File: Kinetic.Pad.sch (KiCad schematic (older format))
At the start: 18 parts, among them SW1 Rotary_Encoder_Switch, U1 ProMicro

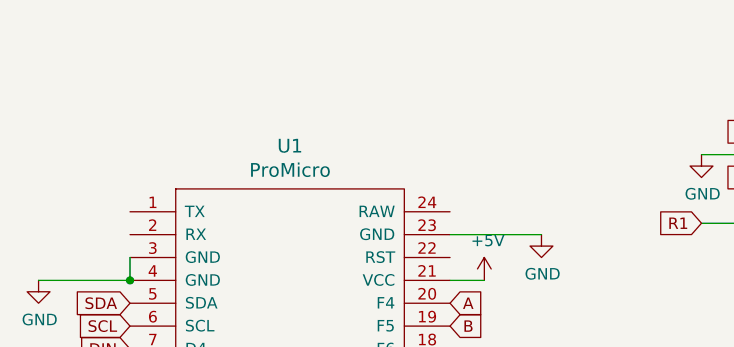
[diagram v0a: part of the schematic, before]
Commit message: Updated MX Libraries
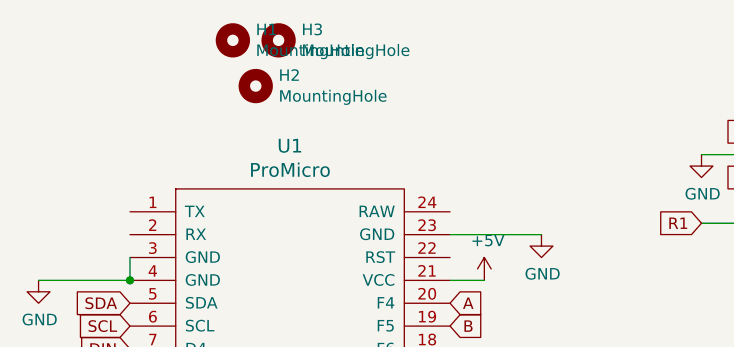
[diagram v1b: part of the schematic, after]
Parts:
- added H1, H2, H3: MountingHole, MountingHole:MountingHole_2mm, symbol Mechanical:MountingHole
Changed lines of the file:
@@
 Wire Wire Line
 	5150 3900 5700 3900
+$Comp
+L Mechanical:MountingHole H1
+U 1 1 61AF6BAE
+P 2350 950
+F 0 "H1" H 2450 996 50  0000 L CNN
+F 1 "MountingHole" H 2450 905 50  0000 L CNN
+F 2 "MountingHole:MountingHole_2mm" H 2350 950 50  0001 C CNN
+F 3 "~" H 2350 950 50  0001 C CNN
+	1    2350 950
+	1    0    0    -1
+$EndComp
+$Comp
+L Mechanical:MountingHole H3
+U 1 1 61AF77EB
+P 2550 950
+F 0 "H3" H 2650 996 50  0000 L CNN
+F 1 "MountingHole" H 2650 905 50  0000 L CNN
+F 2 "MountingHole:MountingHole_2mm" H 2550 950 50  0001 C CNN
+F 3 "~" H 2550 950 50  0001 C CNN
+	1    2550 950
+	1    0    0    -1
+$EndComp
+$Comp
+L Mechanical:MountingHole H2
+U 1 1 61AF7FA8
+P 2450 1150
+F 0 "H2" H 2550 1196 50  0000 L CNN
+F 1 "MountingHole" H 2550 1105 50  0000 L CNN
+F 2 "MountingHole:MountingHole_2mm" H 2450 1150 50  0001 C CNN
+F 3 "~" H 2450 1150 50  0001 C CNN
+	1    2450 1150
+	1    0    0    -1
+$EndComp
 $EndSCHEMATC

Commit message: Switched Libraries, Deleted Old Gerbers, Deleted Old Step FIle
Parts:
- MX1, MX2, MX3, MX4, MX5: footprint MX_Alps_Hybrid:MX-1U-NoLED -> MX_Only:MXOnly-1U-NoLED
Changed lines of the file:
@@
 F 0 "MX1" H 4583 2973 60  0000 C CNN
 F 1 "MX-NoLED" H 4583 2899 20  0000 C CNN
-F 2 "MX_Alps_Hybrid:MX-1U-NoLED" H 3925 2725 60  0001 C CNN
+F 2 "MX_Only:MXOnly-1U-NoLED" H 3925 2725 60  0001 C CNN
 F 3 "" H 3925 2725 60  0001 C CNN
 	1    4550 2750
@@
 F 0 "MX3" H 5033 2973 60  0000 C CNN
 F 1 "MX-NoLED" H 5033 2899 20  0000 C CNN
-F 2 "MX_Alps_Hybrid:MX-1U-NoLED" H 4375 2725 60  0001 C CNN
+F 2 "MX_Only:MXOnly-1U-NoLED" H 4375 2725 60  0001 C CNN
 F 3 "" H 4375 2725 60  0001 C CNN
 	1    5000 2750
@@
 F 0 "MX5" H 5483 2973 60  0000 C CNN
 F 1 "MX-NoLED" H 5483 2899 20  0000 C CNN
-F 2 "MX_Alps_Hybrid:MX-1U-NoLED" H 4825 2725 60  0001 C CNN
+F 2 "MX_Only:MXOnly-1U-NoLED" H 4825 2725 60  0001 C CNN
 F 3 "" H 4825 2725 60  0001 C CNN
 	1    5450 2750
@@
 F 0 "MX4" H 5483 2323 60  0000 C CNN
 F 1 "MX-NoLED" H 5483 2249 20  0000 C CNN
-F 2 "MX_Alps_Hybrid:MX-1U-NoLED" H 4825 2075 60  0001 C CNN
+F 2 "MX_Only:MXOnly-1U-NoLED" H 4825 2075 60  0001 C CNN
 F 3 "" H 4825 2075 60  0001 C CNN
 	1    5450 2100
@@
 F 0 "MX2" H 5033 2323 60  0000 C CNN
 F 1 "MX-NoLED" H 5033 2249 20  0000 C CNN
-F 2 "MX_Alps_Hybrid:MX-1U-NoLED" H 4375 2075 60  0001 C CNN
+F 2 "MX_Only:MXOnly-1U-NoLED" H 4375 2075 60  0001 C CNN
 F 3 "" H 4375 2075 60  0001 C CNN
 	1    5000 2100

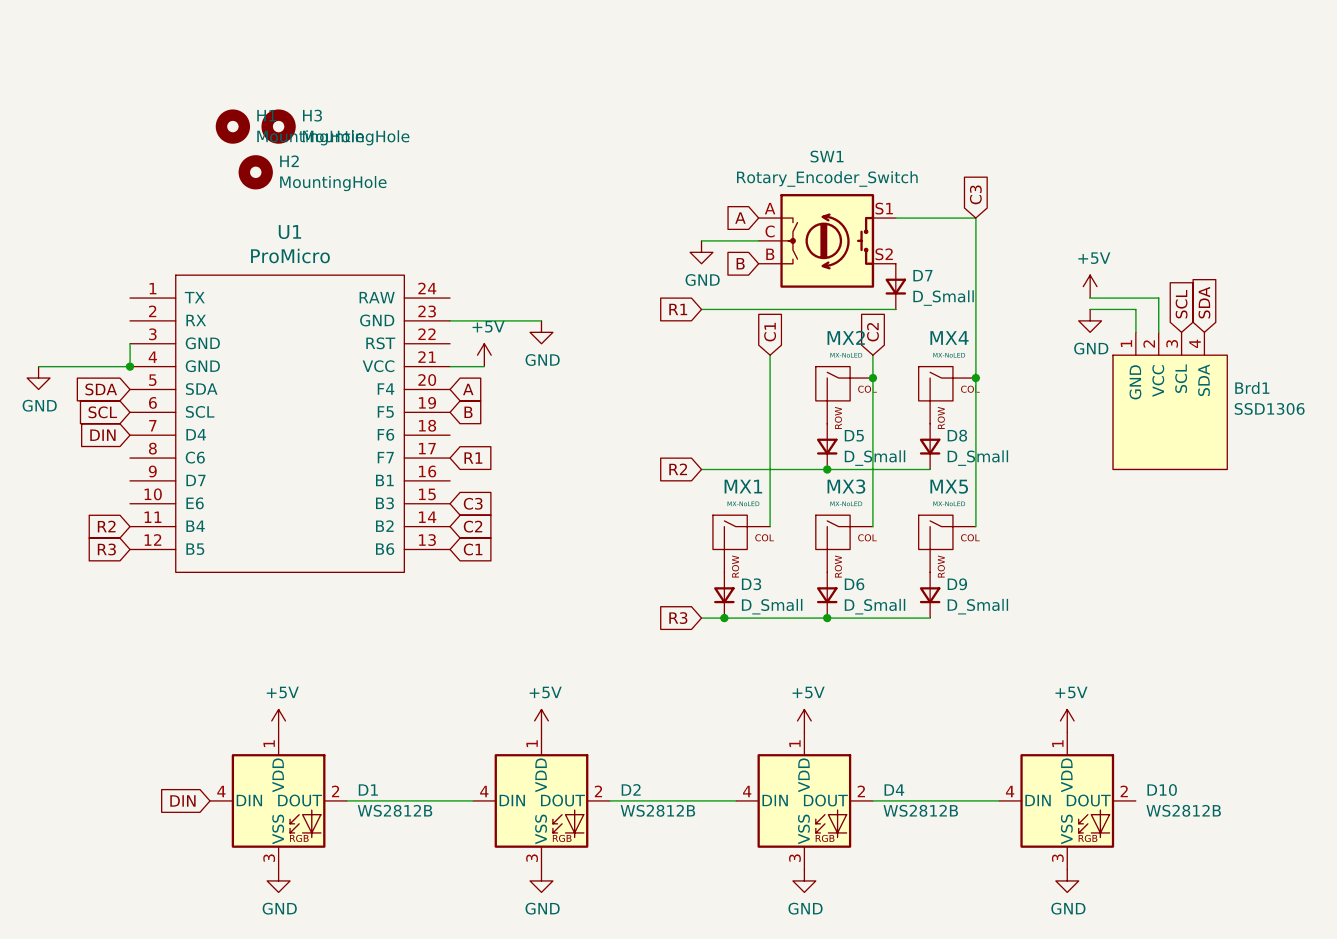
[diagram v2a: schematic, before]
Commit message: Removed Old Gerbers
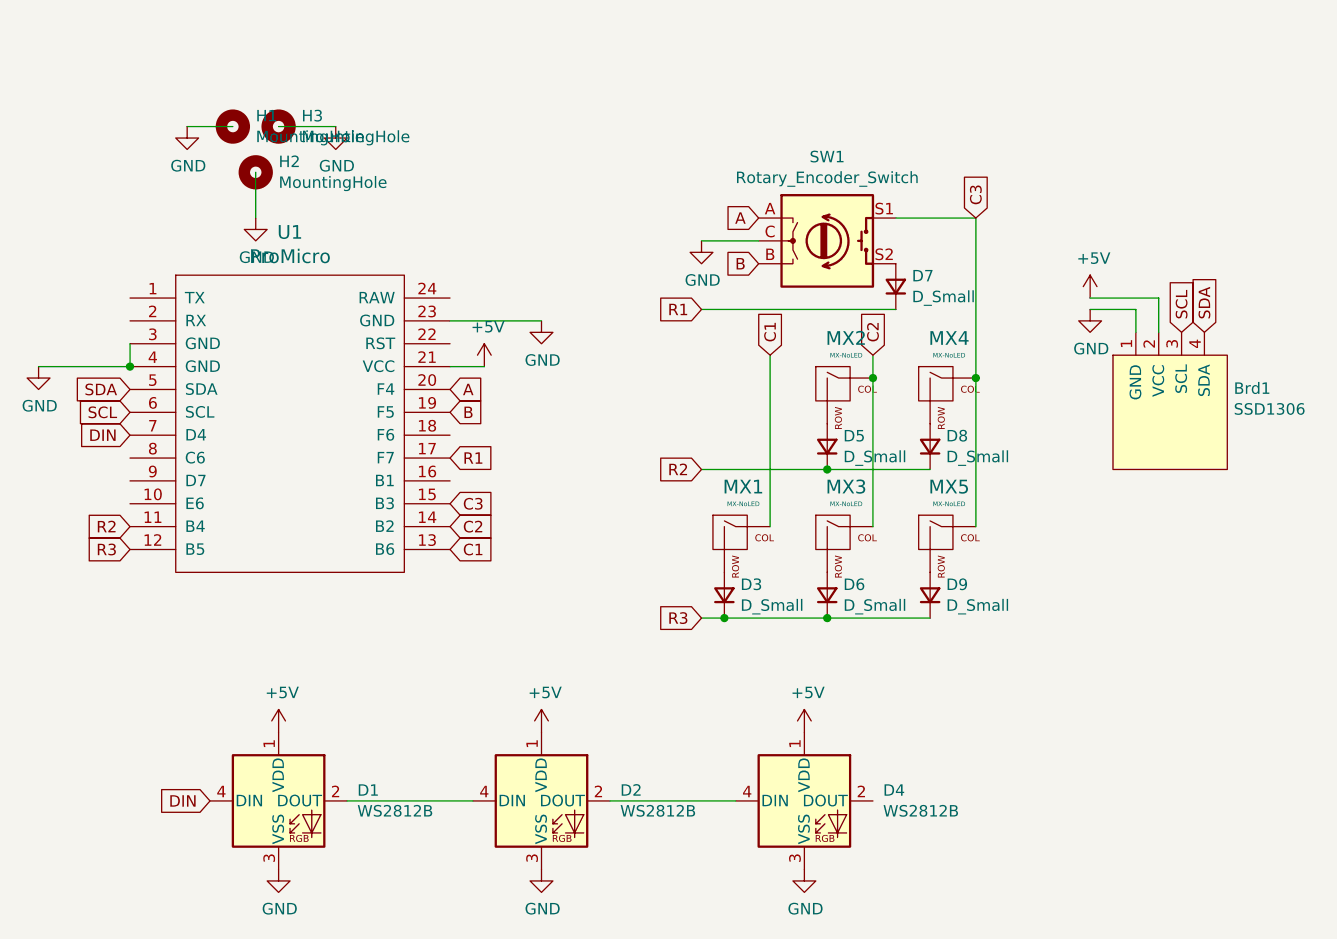
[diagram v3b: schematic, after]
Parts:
- removed D10: WS2812B, LED_SMD:LED_WS2812B_PLCC4_5.0x5.0mm_P3.2mm, symbol LED:WS2812B
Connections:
- wire segments 24 -> 26
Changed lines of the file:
@@
-$EndComp
-$Comp
-L LED:WS2812B D10
-U 1 1 61A89769
-P 6000 3900
-F 0 "D10" H 6344 3946 50  0000 L CNN
-F 1 "WS2812B" H 6344 3855 50  0000 L CNN
-F 2 "LED_SMD:LED_WS2812B_PLCC4_5.0x5.0mm_P3.2mm" H 6050 3600 50  0001 L TNN
-F 3 "https://cdn-shop.adafruit.com/datasheets/WS2812B.pdf" H 6100 3525 50  0001 L TNN
-	1    6000 3900
-	1    0    0    -1
 $EndComp
 $Comp
@@
 F 3 "" H 4850 4200 50  0001 C CNN
 	1    4850 4200
-	1    0    0    -1
-$EndComp
-$Comp
-L power:GND #PWR0110
-U 1 1 61A8B838
-P 6000 4200
-F 0 "#PWR0110" H 6000 3950 50  0001 C CNN
-F 1 "GND" H 6005 4027 50  0000 C CNN
-F 2 "" H 6000 4200 50  0001 C CNN
-F 3 "" H 6000 4200 50  0001 C CNN
-	1    6000 4200
-	1    0    0    -1
-$EndComp
-$Comp
-L power:+5V #PWR0111
-U 1 1 61A8BD21
-P 6000 3600
-F 0 "#PWR0111" H 6000 3450 50  0001 C CNN
-F 1 "+5V" H 6015 3773 50  0000 C CNN
-F 2 "" H 6000 3600 50  0001 C CNN
-F 3 "" H 6000 3600 50  0001 C CNN
-	1    6000 3600
 	1    0    0    -1
 $EndComp
@@
 Wire Wire Line
 	4000 3900 4550 3900
-Wire Wire Line
-	5150 3900 5700 3900
 $Comp
 L Mechanical:MountingHole H1
@@
 	1    0    0    -1
 $EndComp
+Wire Wire Line
+	2550 950  2800 950
+Wire Wire Line
+	2450 1150 2450 1350
+Wire Wire Line
+	2350 950  2150 950
+$Comp
+L power:GND #PWR0110
+U 1 1 61A99687
+P 2800 950
+F 0 "#PWR0110" H 2800 700 50  0001 C CNN
+F 1 "GND" H 2805 777 50  0000 C CNN
+F 2 "" H 2800 950 50  0001 C CNN
+F 3 "" H 2800 950 50  0001 C CNN
+	1    2800 950
+	1    0    0    -1
+$EndComp
+$Comp
+L power:GND #PWR0111
+U 1 1 61A99FC8
+P 2450 1350
+F 0 "#PWR0111" H 2450 1100 50  0001 C CNN
+F 1 "GND" H 2455 1177 50  0000 C CNN
+F 2 "" H 2450 1350 50  0001 C CNN
+F 3 "" H 2450 1350 50  0001 C CNN
+	1    2450 1350
+	1    0    0    -1
+$EndComp
+$Comp
+L power:GND #PWR0115
+U 1 1 61A9A984
+P 2150 950
+F 0 "#PWR0115" H 2150 700 50  0001 C CNN
+F 1 "GND" H 2155 777 50  0000 C CNN
+F 2 "" H 2150 950 50  0001 C CNN
+F 3 "" H 2150 950 50  0001 C CNN
+	1    2150 950
+	1    0    0    -1
+$EndComp

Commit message: Nothing Important
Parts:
- removed H1, H2, H3: MountingHole, MountingHole:MountingHole_2mm, symbol Mechanical:MountingHole
- added H1, H2, H3: MountingHole_Pad, MountingHole:MountingHole_2.5mm_Pad, symbol Mechanical:MountingHole_Pad
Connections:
- wire segments 26 -> 23
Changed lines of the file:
@@
 	4000 3900 4550 3900
 $Comp
-L Mechanical:MountingHole H1
-U 1 1 61AF6BAE
-P 2350 950
-F 0 "H1" H 2450 996 50  0000 L CNN
-F 1 "MountingHole" H 2450 905 50  0000 L CNN
-F 2 "MountingHole:MountingHole_2mm" H 2350 950 50  0001 C CNN
-F 3 "~" H 2350 950 50  0001 C CNN
-	1    2350 950
+L Mechanical:MountingHole_Pad H1
+U 1 1 61A9C773
+P 1700 1050
+F 0 "H1" H 1800 1099 50  0000 L CNN
+F 1 "MountingHole_Pad" H 1800 1008 50  0000 L CNN
+F 2 "MountingHole:MountingHole_2.5mm_Pad" H 1700 1050 50  0001 C CNN
+F 3 "~" H 1700 1050 50  0001 C CNN
+	1    1700 1050
 	1    0    0    -1
 $EndComp
 $Comp
-L Mechanical:MountingHole H3
-U 1 1 61AF77EB
-P 2550 950
-F 0 "H3" H 2650 996 50  0000 L CNN
-F 1 "MountingHole" H 2650 905 50  0000 L CNN
-F 2 "MountingHole:MountingHole_2mm" H 2550 950 50  0001 C CNN
-F 3 "~" H 2550 950 50  0001 C CNN
-	1    2550 950
+L Mechanical:MountingHole_Pad H3
+U 1 1 61A9D1A0
+P 1900 1050
+F 0 "H3" H 2000 1099 50  0000 L CNN
+F 1 "MountingHole_Pad" H 2000 1008 50  0000 L CNN
+F 2 "MountingHole:MountingHole_2.5mm_Pad" H 1900 1050 50  0001 C CNN
+F 3 "~" H 1900 1050 50  0001 C CNN
+	1    1900 1050
 	1    0    0    -1
 $EndComp
 $Comp
-L Mechanical:MountingHole H2
-U 1 1 61AF7FA8
-P 2450 1150
-F 0 "H2" H 2550 1196 50  0000 L CNN
-F 1 "MountingHole" H 2550 1105 50  0000 L CNN
-F 2 "MountingHole:MountingHole_2mm" H 2450 1150 50  0001 C CNN
-F 3 "~" H 2450 1150 50  0001 C CNN
-	1    2450 1150
+L Mechanical:MountingHole_Pad H2
+U 1 1 61A9D90B
+P 1800 600
+F 0 "H2" H 1900 649 50  0000 L CNN
+F 1 "MountingHole_Pad" H 1900 558 50  0000 L CNN
+F 2 "MountingHole:MountingHole_2.5mm_Pad" H 1800 600 50  0001 C CNN
+F 3 "~" H 1800 600 50  0001 C CNN
+	1    1800 600
 	1    0    0    -1
 $EndComp
-Wire Wire Line
-	2550 950  2800 950
-Wire Wire Line
-	2450 1150 2450 1350
-Wire Wire Line
-	2350 950  2150 950
 $Comp
 L power:GND #PWR0110
-U 1 1 61A99687
-P 2800 950
-F 0 "#PWR0110" H 2800 700 50  0001 C CNN
-F 1 "GND" H 2805 777 50  0000 C CNN
-F 2 "" H 2800 950 50  0001 C CNN
-F 3 "" H 2800 950 50  0001 C CNN
-	1    2800 950
+U 1 1 61AA5B29
+P 1700 1150
+F 0 "#PWR0110" H 1700 900 50  0001 C CNN
+F 1 "GND" H 1705 977 50  0000 C CNN
+F 2 "" H 1700 1150 50  0001 C CNN
+F 3 "" H 1700 1150 50  0001 C CNN
+	1    1700 1150
 	1    0    0    -1
 $EndComp
 $Comp
 L power:GND #PWR0111
-U 1 1 61A99FC8
-P 2450 1350
-F 0 "#PWR0111" H 2450 1100 50  0001 C CNN
-F 1 "GND" H 2455 1177 50  0000 C CNN
-F 2 "" H 2450 1350 50  0001 C CNN
-F 3 "" H 2450 1350 50  0001 C CNN
-	1    2450 1350
+U 1 1 61AA6232
+P 1900 1150
+F 0 "#PWR0111" H 1900 900 50  0001 C CNN
+F 1 "GND" H 1905 977 50  0000 C CNN
+F 2 "" H 1900 1150 50  0001 C CNN
+F 3 "" H 1900 1150 50  0001 C CNN
+	1    1900 1150
 	1    0    0    -1
 $EndComp
 $Comp
 L power:GND #PWR0115
-U 1 1 61A9A984
-P 2150 950
-F 0 "#PWR0115" H 2150 700 50  0001 C CNN
-F 1 "GND" H 2155 777 50  0000 C CNN
-F 2 "" H 2150 950 50  0001 C CNN
-F 3 "" H 2150 950 50  0001 C CNN
-	1    2150 950
+U 1 1 61AA723D
+P 1800 700
+F 0 "#PWR0115" H 1800 450 50  0001 C CNN
+F 1 "GND" H 1805 527 50  0000 C CNN
+F 2 "" H 1800 700 50  0001 C CNN
+F 3 "" H 1800 700 50  0001 C CNN
+	1    1800 700
 	1    0    0    -1
 $EndComp
